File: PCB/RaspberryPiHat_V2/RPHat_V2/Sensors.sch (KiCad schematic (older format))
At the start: 12 parts

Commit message: Working on the PCB
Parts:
- added IC?: TXB0108YZPR2, BGA20C50P4X5_189X239X50, symbol TXB0108YZPR2:TXB0108YZPR2
- R? (x2): footprint (none) -> Resistor_SMD:R_0603_1608Metric_Pad0.98x0.95mm_HandSolder
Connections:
- net labels added: BME_CS_18, IMU_CS_18, IMU_INT_18, SPI_CLK_18, SPI_MISO_18, SPI_MOSI_18
- net labels removed: BME_CS, IMU_CS, IMU_INT, SPI_CLK, SPI_MISO, SPI_MOSI
- wire segments 57 -> 59
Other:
- note removed: "Needs logic converter to communicate with teensy"
- moved on the sheet: C?, J?, R?, U?

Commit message: Configured pinout for logic converter
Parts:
- IC?: symbol TXB0108YZPR2:TXB0108YZPR2 -> RPHat_V2-rescue:TXB0108YZPR2-TXB0108YZPR2
- U?: symbol User_Created:GY-NEO6MV2 -> RPHat_V2-rescue:GY-NEO6MV2-User_Created
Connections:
- net labels added: +3V3, BME_CS_33, IMU_CS_33, SPI_CLK_33, SPI_MISO_33, SPI_MOSI_33
- wire segments 59 -> 75
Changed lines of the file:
@@
 $EndComp
 $Comp
-L User_Created:GY-NEO6MV2 U?
+L RPHat_V2-rescue:GY-NEO6MV2-User_Created U?
 U 1 1 60929062
 P 10400 1350
@@
 	2900 2000 3650 2000
 $Comp
-L TXB0108YZPR2:TXB0108YZPR2 IC?
+L RPHat_V2-rescue:TXB0108YZPR2-TXB0108YZPR2 IC?
 U 1 1 60A9D2C1
 P 6450 3800
@@
 	1    0    0    -1
 $EndComp
+$Comp
+L power:+1V8 #PWR?
+U 1 1 609C23EB
+P 8100 3800
+F 0 "#PWR?" H 8100 3650 50  0001 C CNN
+F 1 "+1V8" H 8115 3973 50  0000 C CNN
+F 2 "" H 8100 3800 50  0001 C CNN
+F 3 "" H 8100 3800 50  0001 C CNN
+	1    8100 3800
+	1    0    0    -1
+$EndComp
+$Comp
+L power:+3V3 #PWR?
+U 1 1 609C3DE0
+P 5600 4500
+F 0 "#PWR?" H 5600 4350 50  0001 C CNN
+F 1 "+3V3" H 5615 4673 50  0000 C CNN
+F 2 "" H 5600 4500 50  0001 C CNN
+F 3 "" H 5600 4500 50  0001 C CNN
+	1    5600 4500
+	1    0    0    -1
+$EndComp
+Wire Wire Line
+	5600 4600 5600 4500
+Wire Wire Line
+	8100 3900 8100 3800
+$Comp
+L power:GNDREF #PWR?
+U 1 1 609C7438
+P 8100 4050
+F 0 "#PWR?" H 8100 3800 50  0001 C CNN
+F 1 "GNDREF" H 8105 3877 50  0001 C CNN
+F 2 "" H 8100 4050 50  0001 C CNN
+F 3 "" H 8100 4050 50  0001 C CNN
+	1    8100 4050
+	1    0    0    -1
+$EndComp
+Wire Wire Line
+	8100 4000 8100 4050
+Wire Wire Line
+	7550 3900 8100 3900
+Wire Wire Line
+	7550 4000 8100 4000
+Text GLabel 6350 4000 0    50   Input ~ 0
+SPI_MISO_18
+Text GLabel 6350 4100 0    50   Input ~ 0
+SPI_MOSI_18
+Text GLabel 6350 4400 0    50   Input ~ 0
+SPI_CLK_18
+Text GLabel 6350 4500 0    50   Input ~ 0
+IMU_CS_18
+Text GLabel 7600 3800 2    50   Input ~ 0
+BME_CS_18
+Text GLabel 6350 3900 0    50   Input ~ 0
+SPI_MISO_33
+Text GLabel 6350 3800 0    50   Input ~ 0
+SPI_MOSI_33
+Text GLabel 6350 4300 0    50   Input ~ 0
+SPI_CLK_33
+Text GLabel 6350 4200 0    50   Input ~ 0
+IMU_CS_33
+Text GLabel 6350 4700 0    50   Input ~ 0
+BME_CS_33
+Wire Wire Line
+	5600 4600 6450 4600
+Wire Wire Line
+	7600 3800 7550 3800
+Wire Wire Line
+	6350 4000 6450 4000
+Wire Wire Line
+	6350 4100 6450 4100
+Wire Wire Line
+	6350 4400 6450 4400
+Wire Wire Line
+	6350 4500 6450 4500
+Wire Wire Line
+	6350 3800 6450 3800
+Wire Wire Line
+	6350 3900 6450 3900
+Wire Wire Line
+	6350 4200 6450 4200
+Wire Wire Line
+	6350 4300 6450 4300
+Wire Wire Line
+	6350 4700 6450 4700
 $EndSCHEMATC

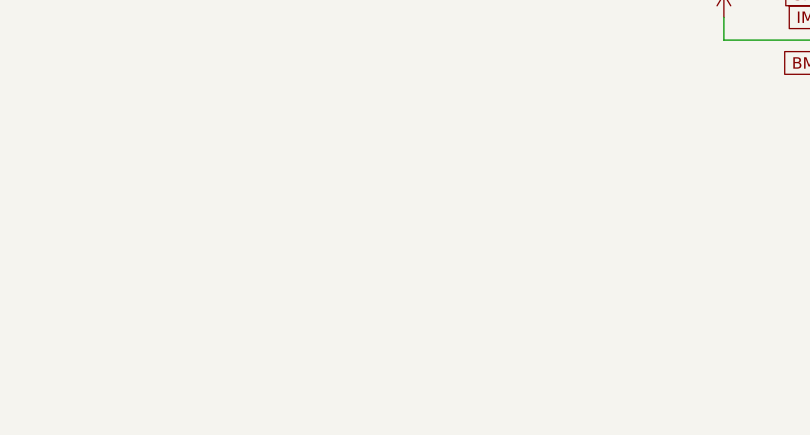
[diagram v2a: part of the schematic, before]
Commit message: Started routing for the BMS
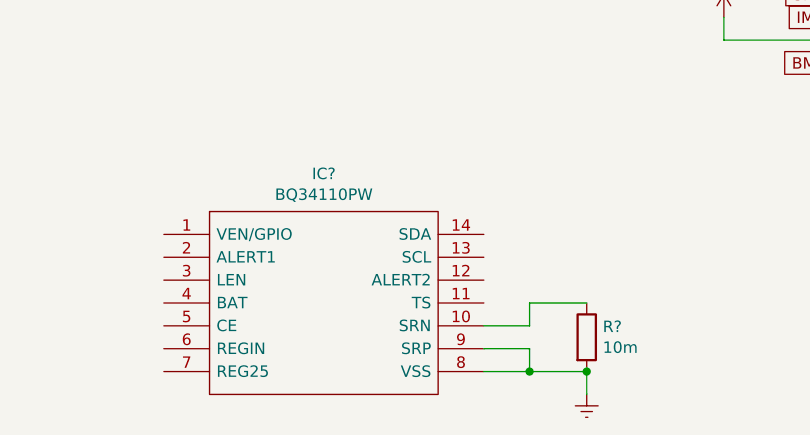
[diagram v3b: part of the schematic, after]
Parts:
- added IC?: BQ34110PW, SOP65P640X120-14N, symbol BQ34110PW:BQ34110PW
- added R?: 10m, symbol Device:R
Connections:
- net GNDREF: now also IC?.8 (VSS), IC?.9 (SRP), R?.2
- new net: IC?.10 (SRN), R?.1
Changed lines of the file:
@@
 Wire Wire Line
 	6350 4700 6450 4700
+$Comp
+L BQ34110PW:BQ34110PW IC?
+U 1 1 609EAECE
+P 3150 5450
+F 0 "IC?" H 3850 5715 50  0000 C CNN
+F 1 "BQ34110PW" H 3850 5624 50  0000 C CNN
+F 2 "SOP65P640X120-14N" H 4400 5550 50  0001 L CNN
+F 3 "http://www.ti.com/lit/gpn/bq34110" H 4400 5450 50  0001 L CNN
+F 4 "Battery Management Multi-Chemistry High-cell Count Battery Fuel Gauge w/Integrated Rarely Discharged Module 14-TSSOP -40 to 85" H 4400 5350 50  0001 L CNN "Description"
+F 5 "1.2" H 4400 5250 50  0001 L CNN "Height"
+F 6 "Texas Instruments" H 4400 5150 50  0001 L CNN "Manufacturer_Name"
+F 7 "BQ34110PW" H 4400 5050 50  0001 L CNN "Manufacturer_Part_Number"
+F 8 "595-BQ34110PW" H 4400 4950 50  0001 L CNN "Mouser Part Number"
+F 9 "https://www.mouser.co.uk/ProductDetail/Texas-Instruments/BQ34110PW?qs=OEYMhS7p3YbAd6vB%252BTGmNQ%3D%3D" H 4400 4850 50  0001 L CNN "Mouser Price/Stock"
+F 10 "BQ34110PW" H 4400 4750 50  0001 L CNN "Arrow Part Number"
+F 11 "https://www.arrow.com/en/products/bq34110pw/texas-instruments" H 4400 4650 50  0001 L CNN "Arrow Price/Stock"
+	1    3150 5450
+	1    0    0    -1
+$EndComp
+$Comp
+L Device:R R?
+U 1 1 609ED767
+P 5000 5900
+F 0 "R?" H 5070 5946 50  0000 L CNN
+F 1 "10m" H 5070 5855 50  0000 L CNN
+F 2 "" V 4930 5900 50  0001 C CNN
+F 3 "~" H 5000 5900 50  0001 C CNN
+	1    5000 5900
+	1    0    0    -1
+$EndComp
+Wire Wire Line
+	4550 5850 4750 5850
+Wire Wire Line
+	4750 5850 4750 5750
+Wire Wire Line
+	4750 5750 5000 5750
+Wire Wire Line
+	5000 6050 4750 6050
+Wire Wire Line
+	4750 6050 4750 5950
+Wire Wire Line
+	4750 5950 4550 5950
+Wire Wire Line
+	4550 6050 4750 6050
+Connection ~ 4750 6050
+$Comp
+L power:GNDREF #PWR?
+U 1 1 609F7B72
+P 5000 6150
+F 0 "#PWR?" H 5000 5900 50  0001 C CNN
+F 1 "GNDREF" H 5005 5977 50  0001 C CNN
+F 2 "" H 5000 6150 50  0001 C CNN
+F 3 "" H 5000 6150 50  0001 C CNN
+	1    5000 6150
+	1    0    0    -1
+$EndComp
+Wire Wire Line
+	5000 6050 5000 6150
+Connection ~ 5000 6050
 $EndSCHEMATC

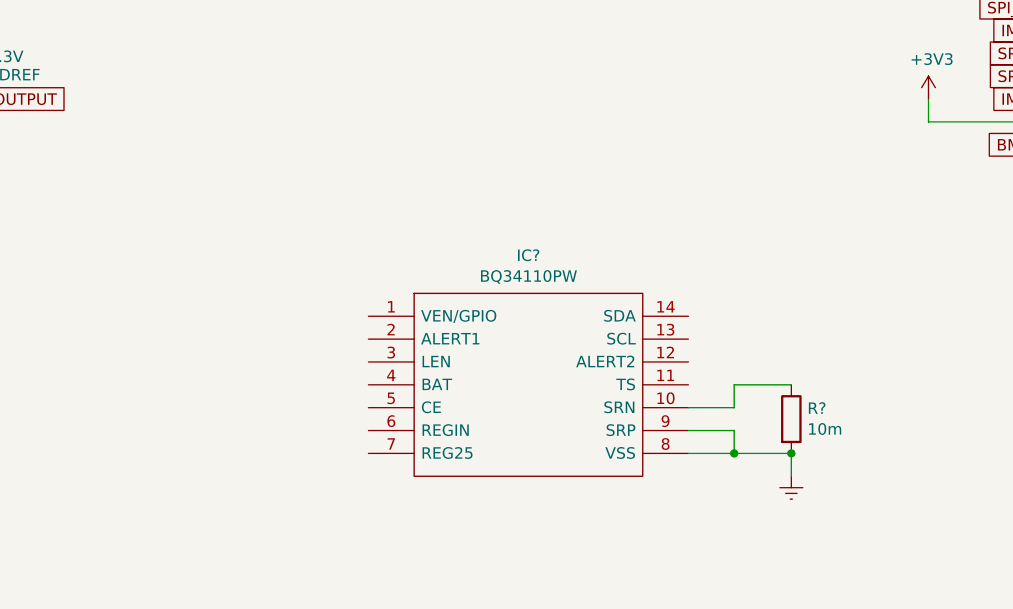
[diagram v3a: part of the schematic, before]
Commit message: Continued routing the pcb. Added current sensing sensor
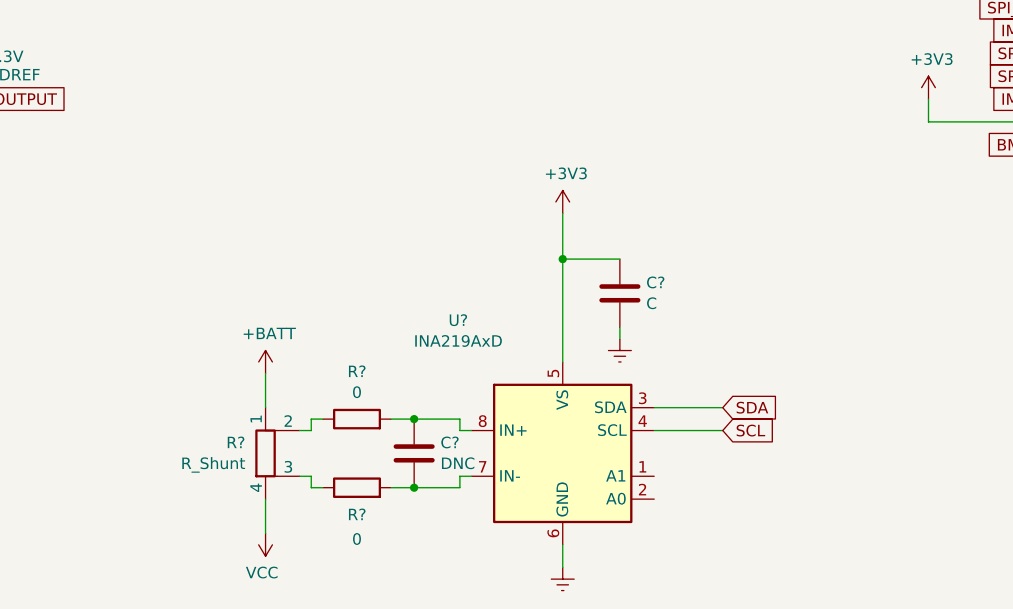
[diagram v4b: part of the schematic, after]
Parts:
- removed IC?: BQ34110PW, SOP65P640X120-14N, symbol BQ34110PW:BQ34110PW
- removed R?: 10m, symbol Device:R
- added C?: C, symbol Device:C
- added C?: DNC, symbol Device:C
- added R?: R_Shunt, symbol Device:R_Shunt
- added R? (x2): 0, symbol Device:R
- added U?: INA219AxD, Package_SO:SOIC-8_3.9x4.9mm_P1.27mm, symbol Analog_ADC:INA219AxD
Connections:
- net +3V3: now also C?.1, U?.5 (VS)
- net GNDREF: now also C?.2, U?.6 (GND)
- new net: C?.2, R?.2, U?.7 (IN-)
- new net: C?.1, R?.2, U?.8 (IN+)
- new net: R?.1, R?.2
- new net: R?.1, R?.3
- new net +BATT: R?.1
- new net SCL: U?.4 (SCL)
- new net SDA: U?.3 (SDA)
- new net VCC: R?.4
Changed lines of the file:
@@
 Wire Wire Line
 	6350 4700 6450 4700
+Text GLabel 4700 5850 2    50   Input ~ 0
+SDA
+Text GLabel 4700 5950 2    50   Input ~ 0
+SCL
+Wire Wire Line
+	4700 5850 4400 5850
+Wire Wire Line
+	4400 5950 4700 5950
 $Comp
-L BQ34110PW:BQ34110PW IC?
-U 1 1 609EAECE
-P 3150 5450
-F 0 "IC?" H 3850 5715 50  0000 C CNN
-F 1 "BQ34110PW" H 3850 5624 50  0000 C CNN
-F 2 "SOP65P640X120-14N" H 4400 5550 50  0001 L CNN
-F 3 "http://www.ti.com/lit/gpn/bq34110" H 4400 5450 50  0001 L CNN
-F 4 "Battery Management Multi-Chemistry High-cell Count Battery Fuel Gauge w/Integrated Rarely Discharged Module 14-TSSOP -40 to 85" H 4400 5350 50  0001 L CNN "Description"
-F 5 "1.2" H 4400 5250 50  0001 L CNN "Height"
-F 6 "Texas Instruments" H 4400 5150 50  0001 L CNN "Manufacturer_Name"
-F 7 "BQ34110PW" H 4400 5050 50  0001 L CNN "Manufacturer_Part_Number"
-F 8 "595-BQ34110PW" H 4400 4950 50  0001 L CNN "Mouser Part Number"
-F 9 "https://www.mouser.co.uk/ProductDetail/Texas-Instruments/BQ34110PW?qs=OEYMhS7p3YbAd6vB%252BTGmNQ%3D%3D" H 4400 4850 50  0001 L CNN "Mouser Price/Stock"
-F 10 "BQ34110PW" H 4400 4750 50  0001 L CNN "Arrow Part Number"
-F 11 "https://www.arrow.com/en/products/bq34110pw/texas-instruments" H 4400 4650 50  0001 L CNN "Arrow Price/Stock"
-	1    3150 5450
+L power:GNDREF #PWR?
+U 1 1 60A1DE54
+P 4000 6550
+F 0 "#PWR?" H 4000 6300 50  0001 C CNN
+F 1 "GNDREF" H 4005 6377 50  0001 C CNN
+F 2 "" H 4000 6550 50  0001 C CNN
+F 3 "" H 4000 6550 50  0001 C CNN
+	1    4000 6550
+	1    0    0    -1
+$EndComp
+$Comp
+L Analog_ADC:INA219AxD U?
+U 1 1 60A1725E
+P 4000 6050
+F 0 "U?" H 3543 6631 50  0000 C CNN
+F 1 "INA219AxD" H 3543 6540 50  0000 C CNN
+F 2 "Package_SO:SOIC-8_3.9x4.9mm_P1.27mm" H 4800 5700 50  0001 C CNN
+F 3 "http://www.ti.com/lit/ds/symlink/ina219.pdf" H 4350 5950 50  0001 C CNN
+	1    4000 6050
+	1    0    0    -1
+$EndComp
+$Comp
+L Device:C C?
+U 1 1 60A1ED8C
+P 4250 5350
+F 0 "C?" H 4365 5396 50  0000 L CNN
+F 1 "C" H 4365 5305 50  0000 L CNN
+F 2 "" H 4288 5200 50  0001 C CNN
+F 3 "~" H 4250 5350 50  0001 C CNN
+	1    4250 5350
+	1    0    0    -1
+$EndComp
+$Comp
+L power:+3V3 #PWR?
+U 1 1 60A2003A
+P 4000 5000
+F 0 "#PWR?" H 4000 4850 50  0001 C CNN
+F 1 "+3V3" H 4015 5173 50  0000 C CNN
+F 2 "" H 4000 5000 50  0001 C CNN
+F 3 "" H 4000 5000 50  0001 C CNN
+	1    4000 5000
+	1    0    0    -1
+$EndComp
+Wire Wire Line
+	4000 5000 4000 5200
+Wire Wire Line
+	4250 5200 4000 5200
+Connection ~ 4000 5200
+Wire Wire Line
+	4000 5200 4000 5650
+$Comp
+L power:GNDREF #PWR?
+U 1 1 60A25263
+P 4250 5550
+F 0 "#PWR?" H 4250 5300 50  0001 C CNN
+F 1 "GNDREF" H 4255 5377 50  0001 C CNN
+F 2 "" H 4250 5550 50  0001 C CNN
+F 3 "" H 4250 5550 50  0001 C CNN
+	1    4250 5550
+	1    0    0    -1
+$EndComp
+Wire Wire Line
+	4250 5500 4250 5550
+$Comp
+L Device:R_Shunt R?
+U 1 1 60A2AE3C
+P 2700 6050
+F 0 "R?" H 2612 6096 50  0000 R CNN
+F 1 "R_Shunt" H 2612 6005 50  0000 R CNN
+F 2 "" V 2630 6050 50  0001 C CNN
+F 3 "~" H 2700 6050 50  0001 C CNN
+	1    2700 6050
 	1    0    0    -1
 $EndComp
 $Comp
 L Device:R R?
-U 1 1 609ED767
-P 5000 5900
-F 0 "R?" H 5070 5946 50  0000 L CNN
-F 1 "10m" H 5070 5855 50  0000 L CNN
-F 2 "" V 4930 5900 50  0001 C CNN
-F 3 "~" H 5000 5900 50  0001 C CNN
-	1    5000 5900
+U 1 1 60A32138
+P 3100 5900
+F 0 "R?" V 3307 5900 50  0000 C CNN
+F 1 "0" V 3216 5900 50  0000 C CNN
+F 2 "" V 3030 5900 50  0001 C CNN
+F 3 "~" H 3100 5900 50  0001 C CNN
+	1    3100 5900
+	0    -1   -1   0
+$EndComp
+$Comp
+L Device:R R?
+U 1 1 60A331B9
+P 3100 6200
+F 0 "R?" V 2981 6200 50  0000 C CNN
+F 1 "0" V 2903 6200 50  0000 C BNN
+F 2 "" V 3030 6200 50  0001 C CNN
+F 3 "~" H 3100 6200 50  0001 C CNN
+	1    3100 6200
+	0    -1   -1   0
+$EndComp
+$Comp
+L Device:C C?
+U 1 1 60A408CD
+P 3350 6050
+F 0 "C?" H 3465 6096 50  0000 L CNN
+F 1 "DNC" H 3465 6005 50  0000 L CNN
+F 2 "" H 3388 5900 50  0001 C CNN
+F 3 "~" H 3350 6050 50  0001 C CNN
+	1    3350 6050
 	1    0    0    -1
 $EndComp
 Wire Wire Line
-	4550 5850 4750 5850
+	2850 6150 2900 6150
 Wire Wire Line
-	4750 5850 4750 5750
+	2900 6150 2900 6200
 Wire Wire Line
-	4750 5750 5000 5750
+	2900 6200 2950 6200
 Wire Wire Line
-	5000 6050 4750 6050
+	2850 5950 2900 5950
 Wire Wire Line
-	4750 6050 4750 5950
+	2900 5950 2900 5900
 Wire Wire Line
-	4750 5950 4550 5950
+	2900 5900 2950 5900
 Wire Wire Line
-	4550 6050 4750 6050
-Connection ~ 4750 6050
+	3250 5900 3350 5900
+Wire Wire Line
+	3550 5900 3550 5950
+Wire Wire Line
+	3550 5950 3600 5950
+Connection ~ 3350 5900
+Wire Wire Line
+	3350 5900 3550 5900
+Wire Wire Line
+	3250 6200 3350 6200
+Wire Wire Line
+	3550 6200 3550 6150
+Wire Wire Line
+	3550 6150 3600 6150
+Connection ~ 3350 6200
+Wire Wire Line
+	3350 6200 3550 6200
+Wire Wire Line
+	4000 6450 4000 6550
 $Comp
-L power:GNDREF #PWR?
-U 1 1 609F7B72
-P 5000 6150
-F 0 "#PWR?" H 5000 5900 50  0001 C CNN
-F 1 "GNDREF" H 5005 5977 50  0001 C CNN
-F 2 "" H 5000 6150 50  0001 C CNN
-F 3 "" H 5000 6150 50  0001 C CNN
-	1    5000 6150
+L power:+BATT #PWR?
+U 1 1 60A576AA
+P 2700 5700
+F 0 "#PWR?" H 2700 5550 50  0001 C CNN
+F 1 "+BATT" H 2715 5873 50  0000 C CNN
+F 2 "" H 2700 5700 50  0001 C CNN
+F 3 "" H 2700 5700 50  0001 C CNN
+	1    2700 5700
 	1    0    0    -1
 $EndComp
 Wire Wire Line
-	5000 6050 5000 6150
-Connection ~ 5000 6050
+	2700 5700 2700 5850
+$Comp
+L power:VCC #PWR?
+U 1 1 60A5EBF9
+P 2700 6400
+F 0 "#PWR?" H 2700 6250 50  0001 C CNN
+F 1 "VCC" H 2715 6573 50  0000 C CNN
+F 2 "" H 2700 6400 50  0001 C CNN
+F 3 "" H 2700 6400 50  0001 C CNN
+	1    2700 6400
+	-1   0    0    1
+$EndComp
+Wire Wire Line
+	2700 6250 2700 6400
 $EndSCHEMATC
